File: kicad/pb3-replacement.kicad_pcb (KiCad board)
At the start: 2 copper layers, 0 parts

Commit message: Create PB-3 PCB layout and KiBot outputs
Co-authored-by: donnels <14863623+donnels@users.noreply.github.com>
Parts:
- added BT1: LiPo_3.7V_500-1500mAh, Battery:LiPo_68x17.8mm, B.Cu at (151.0, 108.9)
- added J1: USB_C_5V_IN, Connector_USB:USB_C_Receptacle_USB2.0, F.Cu at (104.0, 108.9)
- added J2: AIWA_DECK_2.4V, Connector:Conn_01x02_Pin, F.Cu at (163.0, 108.9)
- added Q1: FS8205A, Package_TO_SOT_SMD:SOT-23-6, F.Cu at (131.0, 108.9)
- added U1: TP4056, Package_SO:SOIC-8_3.9x4.9mm_P1.27mm, F.Cu at (115.0, 108.9)
- added U2: DW01A, Package_TO_SOT_SMD:SOT-23-6, F.Cu at (124.0, 108.9)
- added U3: TPS61023_2.4V, Regulator_Switching:SOT-23-5, F.Cu at (141.0, 108.9)
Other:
- board outline added: 68 x 17.8 mm
- board text added: "68 x 17.8 mm"
- board text added: "AIWA PB-3 1S LiPo / 2.4 V"
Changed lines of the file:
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@@
-(kicad_pcb (version 20240108) (generator "GitHub Copilot")
-  (general (thickness 1.6))
+(kicad_pcb (version 20240108) (generator pcbnew)
+  (general (thickness 0.8))
   (paper "A4")
   (title_block
-    (title "PB-3 Replacement Gauge")
+    (title "AIWA PB-3 LiPo Replacement")
     (company "AIWA HS-PC202MII")
-    (rev "V0.1")
-    (comment 1 "Outline only. Populate once donor measurements confirmed."))
+    (rev "0.1")
+    (comment 1 "68 x 17.8 mm prototype board; verify connector pinout before fabrication"))
   (layers
     (0 "F.Cu" signal)
     (31 "B.Cu" signal)
-    (34 "Edge.Cuts" user))
+    (36 "B.SilkS" user "b.silkscreen")
+    (37 "F.SilkS" user "f.silkscreen")
+    (44 "Edge.Cuts" user))
   (setup
-    (stackup
-      (layer "F.Cu" (type "signal"))
-      (layer "dielectric 1" (type "dielectric") (thickness 1.5))
-      (layer "B.Cu" (type "signal")))
-    (grid_origin 0 0)
-  )
+    (pad_to_mask_clearance 0)
+    (allow_soldermask_bridges_in_footprints no)
+    (pcbplotparams
+      (layerselection 0x00010fc_ffffffff)
+      (plot_on_all_layers_selection 0x0000000_00000000)
+      (disableapertmacros no)
+      (usegerberextensions yes)
+      (usegerberattributes yes)
+      (usegerberadvancedattributes yes)
+      (creategerberjobfile yes)
+      (dashed_line_dash_ratio 12)
+      (dashed_line_gap_ratio 3)
+      (svgprecision 4)
+      (plotframeref no)
+      (viasonmask no)
+      (mode 1)
+      (useauxorigin no)
+      (hpglpennumber 1)
+      (hpglpenspeed 20)
+      (hpglpendiameter 15)
+      (psnegative no)
+      (psa4output no)
+      (plotreference yes)
+      (plotvalue yes)
+      (plotfptext yes)
+      (plotinvisibletext no)
+      (sketchpadsonfab no)
+      (subtractmaskfromsilk no)
+      (outputformat 1)
+      (mirror no)
+      (drillshape 0)
+      (scaleselection 1)
+      (outputdirectory "fabrication/")))
+  (gr_rect (start 100 100) (end 168 117.8) (stroke (width 0.15) (type default)) (fill none) (layer "Edge.Cuts"))
+  (gr_text "AIWA PB-3  1S LiPo / 2.4 V" (at 134 102.2) (layer "F.SilkS")
+    (effects (font (size 1 1) (thickness 0.15))))
+  (gr_text "68 x 17.8 mm" (at 134 115.8) (layer "B.SilkS")
+    (effects (font (size 0.8 0.8) (thickness 0.12)) (justify mirror)))
+  (footprint "Connector_USB:USB_C_Receptacle_USB2.0" (layer "F.Cu") (at 104 108.9)
+    (property "Reference" "J1" (at 0 -4 0) (layer "F.SilkS") (effects (font (size 1 1) (thickness 0.15))))
+    (property "Value" "USB_C_5V_IN" (at 0 4 0) (layer "F.Fab") hide (effects (font (size 1 1) (thickness 0.15))))
+    (fp_rect (start -3 -2.5) (end 3 2.5) (stroke (width 0.15) (type default)) (fill none) (layer "F.SilkS"))
+    (pad "1" thru_hole rect (at -1.5 0) (size 1.8 1.8) (drill 1) (layers "*.Cu" "*.Mask"))
+    (pad "2" thru_hole circle (at 1.5 0) (size 1.8 1.8) (drill 1) (layers "*.Cu" "*.Mask")))
+  (footprint "Package_SO:SOIC-8_3.9x4.9mm_P1.27mm" (layer "F.Cu") (at 115 108.9)
+    (property "Reference" "U1" (at 0 -3.2 0) (layer "F.SilkS") (effects (font (size 1 1) (thickness 0.15))))
+    (property "Value" "TP4056" (at 0 3.2 0) (layer "F.Fab") hide (effects (font (size 1 1) (thickness 0.15))))
+    (fp_rect (start -2.4 -2.1) (end 2.4 2.1) (stroke (width 0.15) (type default)) (fill none) (layer "F.SilkS"))
+    (pad "1" smd roundrect (at -2.4 -1.905) (size 1.5 0.6) (layers "F.Cu" "F.Paste" "F.Mask") (roundrect_rratio 0.2))
+    (pad "2" smd roundrect (at -2.4 -0.635) (size 1.5 0.6) (layers "F.Cu" "F.Paste" "F.Mask") (roundrect_rratio 0.2))
+    (pad "3" smd roundrect (at -2.4 0.635) (size 1.5 0.6) (layers "F.Cu" "F.Paste" "F.Mask") (roundrect_rratio 0.2))
+    (pad "4" smd roundrect (at -2.4 1.905) (size 1.5 0.6) (layers "F.Cu" "F.Paste" "F.Mask") (roundrect_rratio 0.2))
+    (pad "5" smd roundrect (at 2.4 1.905) (size 1.5 0.6) (layers "F.Cu" "F.Paste" "F.Mask") (roundrect_rratio 0.2))
+    (pad "6" smd roundrect (at 2.4 0.635) (size 1.5 0.6) (layers "F.Cu" "F.Paste" "F.Mask") (roundrect_rratio 0.2))
+    (pad "7" smd roundrect (at 2.4 -0.635) (size 1.5 0.6) (layers "F.Cu" "F.Paste" "F.Mask") (roundrect_rratio 0.2))
+    (pad "8" smd roundrect (at 2.4 -1.905) (size 1.5 0.6) (layers "F.Cu" "F.Paste" "F.Mask") (roundrect_rratio 0.2)))
+  (footprint "Package_TO_SOT_SMD:SOT-23-6" (layer "F.Cu") (at 124 108.9)
+    (property "Reference" "U2" (at 0 -2.5 0) (layer "F.SilkS") (effects (font (size 1 1) (thickness 0.15))))
+    (property "Value" "DW01A" (at 0 2.5 0) (layer "F.Fab") hide (effects (font (size 1 1) (thickness 0.15))))
+    (fp_rect (start -1.6 -1.3) (end 1.6 1.3) (stroke (width 0.15) (type default)) (fill none) (layer "F.SilkS"))
+    (pad "1" smd roundrect (at -1.1 -1.1) (size 1.2 0.6) (layers "F.Cu" "F.Paste" "F.Mask") (roundrect_rratio 0.2))
+    (pad "2" smd roundrect (at -1.1 0) (size 1.2 0.6) (layers "F.Cu" "F.Paste" "F.Mask") (roundrect_rratio 0.2))
+    (pad "3" smd roundrect (at -1.1 1.1) (size 1.2 0.6) (layers "F.Cu" "F.Paste" "F.Mask") (roundrect_rratio 0.2))
+    (pad "4" smd roundrect (at 1.1 1.1) (size 1.2 0.6) (layers "F.Cu" "F.Paste" "F.Mask") (roundrect_rratio 0.2))
+    (pad "5" smd roundrect (at 1.1 0) (size 1.2 0.6) (layers "F.Cu" "F.Paste" "F.Mask") (roundrect_rratio 0.2))
+    (pad "6" smd roundrect (at 1.1 -1.1) (size 1.2 0.6) (layers "F.Cu" "F.Paste" "F.Mask") (roundrect_rratio 0.2)))
+  (footprint "Package_TO_SOT_SMD:SOT-23-6" (layer "F.Cu") (at 131 108.9)
+    (property "Reference" "Q1" (at 0 -2.5 0) (layer "F.SilkS") (effects (font (size 1 1) (thickness 0.15))))
+    (property "Value" "FS8205A" (at 0 2.5 0) (layer "F.Fab") hide (effects (font (size 1 1) (thickness 0.15))))
+    (fp_rect (start -1.6 -1.3) (end 1.6 1.3) (stroke (width 0.15) (type default)) (fill none) (layer "F.SilkS"))
+    (pad "1" smd roundrect (at -1.1 -1.1) (size 1.2 0.6) (layers "F.Cu" "F.Paste" "F.Mask") (roundrect_rratio 0.2))
+    (pad "2" smd roundrect (at -1.1 0) (size 1.2 0.6) (layers "F.Cu" "F.Paste" "F.Mask") (roundrect_rratio 0.2))
+    (pad "3" smd roundrect (at -1.1 1.1) (size 1.2 0.6) (layers "F.Cu" "F.Paste" "F.Mask") (roundrect_rratio 0.2))
+    (pad "4" smd roundrect (at 1.1 1.1) (size 1.2 0.6) (layers "F.Cu" "F.Paste" "F.Mask") (roundrect_rratio 0.2))
+    (pad "5" smd roundrect (at 1.1 0) (size 1.2 0.6) (layers "F.Cu" "F.Paste" "F.Mask") (roundrect_rratio 0.2))
+    (pad "6" smd roundrect (at 1.1 -1.1) (size 1.2 0.6) (layers "F.Cu" "F.Paste" "F.Mask") (roundrect_rratio 0.2)))
+  (footprint "Regulator_Switching:SOT-23-5" (layer "F.Cu") (at 141 108.9)
+    (property "Reference" "U3" (at 0 -2.5 0) (layer "F.SilkS") (effects (font (size 1 1) (thickness 0.15))))
+    (property "Value" "TPS61023_2.4V" (at 0 2.5 0) (layer "F.Fab") hide (effects (font (size 1 1) (thickness 0.15))))
+    (fp_rect (start -1.6 -1.3) (end 1.6 1.3) (stroke (width 0.15) (type default)) (fill none) (layer "F.SilkS"))
+    (pad "1" smd roundrect (at -1.1 -1.1) (size 1.2 0.6) (layers "F.Cu" "F.Paste" "F.Mask") (roundrect_rratio 0.2))
+    (pad "2" smd roundrect (at -1.1 0) (size 1.2 0.6) (layers "F.Cu" "F.Paste" "F.Mask") (roundrect_rratio 0.2))
+    (pad "3" smd roundrect (at -1.1 1.1) (size 1.2 0.6) (layers "F.Cu" "F.Paste" "F.Mask") (roundrect_rratio 0.2))
+    (pad "4" smd roundrect (at 1.1 1.1) (size 1.2 0.6) (layers "F.Cu" "F.Paste" "F.Mask") (roundrect_rratio 0.2))
+    (pad "5" smd roundrect (at 1.1 0) (size 1.2 0.6) (layers "F.Cu" "F.Paste" "F.Mask") (roundrect_rratio 0.2)))
+  (footprint "Connector:Conn_01x02_Pin" (layer "F.Cu") (at 163 108.9)
+    (property "Reference" "J2" (at 0 -3 0) (layer "F.SilkS") (effects (font (size 1 1) (thickness 0.15))))
+    (property "Value" "AIWA_DECK_2.4V" (at 0 3 0) (layer "F.Fab") hide (effects (font (size 1 1) (thickness 0.15))))
+    (fp_rect (start -2 -2) (end 2 2) (stroke (width 0.15) (type default)) (fill none) (layer "F.SilkS"))
+    (pad "1" thru_hole rect (at 0 -1.27) (size 2 2) (drill 1) (layers "*.Cu" "*.Mask"))
+    (pad "2" thru_hole circle (at 0 1.27) (size 2 2) (drill 1) (layers "*.Cu" "*.Mask")))
+  (footprint "Battery:LiPo_68x17.8mm" (layer "B.Cu") (at 151 108.9)
+    (property "Reference" "BT1" (at 0 -5.5 0) (layer "B.SilkS") (effects (font (size 1 1) (thickness 0.15)) (justify mirror)))
+    (property "Value" "LiPo_3.7V_500-1500mAh" (at 0 5.5 0) (layer "B.Fab") hide (effects (font (size 1 1) (thickness 0.15)) (justify mirror)))
+    (fp_rect (start -8 -3.5) (end 8 3.5) (stroke (width 0.15) (type default)) (fill none) (layer "B.SilkS"))
+    (pad "1" thru_hole rect (at -6 0) (size 2 2) (drill 1) (layers "*.Cu" "*.Mask"))
+    (pad "2" thru_hole circle (at 6 0) (size 2 2) (drill 1) (layers "*.Cu" "*.Mask")))
 )

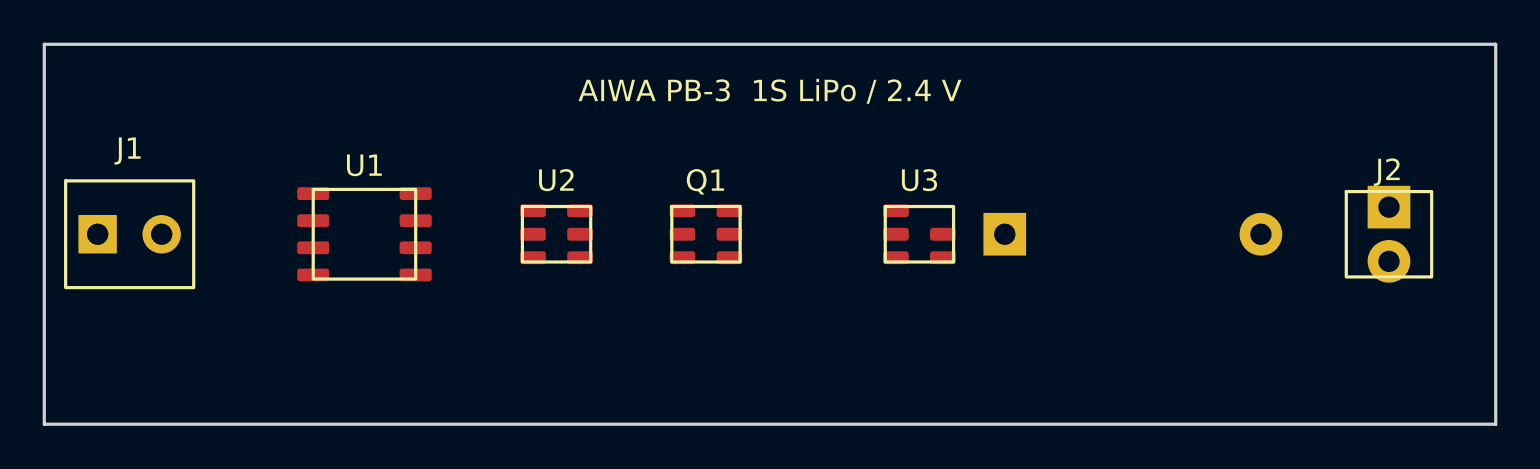
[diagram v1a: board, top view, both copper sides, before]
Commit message: Finalize DRC-clean PB-3 board layout
Co-authored-by: donnels <14863623+donnels@users.noreply.github.com>
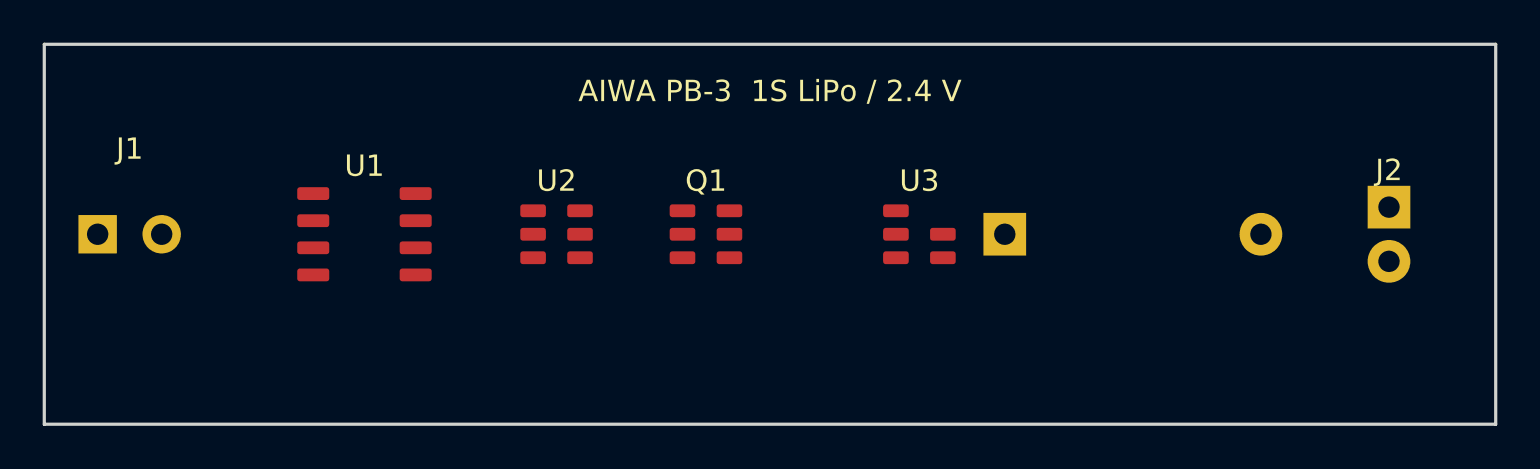
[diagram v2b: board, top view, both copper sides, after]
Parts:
- BT1: footprint Battery:LiPo_68x17.8mm -> PB3_LIPO_68x17.8mm
- J1: footprint Connector_USB:USB_C_Receptacle_USB2.0 -> PB3_USB_C
- J2: footprint Connector:Conn_01x02_Pin -> PB3_DECK_CONNECTOR
- Q1: footprint Package_TO_SOT_SMD:SOT-23-6 -> PB3_FS8205A_SOT23-6
- U1: footprint Package_SO:SOIC-8_3.9x4.9mm_P1.27mm -> PB3_TP4056_SOIC8
- U2: footprint Package_TO_SOT_SMD:SOT-23-6 -> PB3_DW01A_SOT23-6
- U3: footprint Regulator_Switching:SOT-23-5 -> PB3_TPS61023_SOT23-5
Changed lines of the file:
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@@
     (36 "B.SilkS" user "b.silkscreen")
     (37 "F.SilkS" user "f.silkscreen")
+    (49 "F.Fab" user)
     (44 "Edge.Cuts" user))
   (setup
@@
   (gr_text "68 x 17.8 mm" (at 134 115.8) (layer "B.SilkS")
     (effects (font (size 0.8 0.8) (thickness 0.12)) (justify mirror)))
-  (footprint "Connector_USB:USB_C_Receptacle_USB2.0" (layer "F.Cu") (at 104 108.9)
+  (footprint "PB3_USB_C" (layer "F.Cu") (at 104 108.9)
     (property "Reference" "J1" (at 0 -4 0) (layer "F.SilkS") (effects (font (size 1 1) (thickness 0.15))))
     (property "Value" "USB_C_5V_IN" (at 0 4 0) (layer "F.Fab") hide (effects (font (size 1 1) (thickness 0.15))))
-    (fp_rect (start -3 -2.5) (end 3 2.5) (stroke (width 0.15) (type default)) (fill none) (layer "F.SilkS"))
+    (fp_rect (start -3 -2.5) (end 3 2.5) (stroke (width 0.15) (type default)) (fill none) (layer "F.Fab"))
     (pad "1" thru_hole rect (at -1.5 0) (size 1.8 1.8) (drill 1) (layers "*.Cu" "*.Mask"))
     (pad "2" thru_hole circle (at 1.5 0) (size 1.8 1.8) (drill 1) (layers "*.Cu" "*.Mask")))
-  (footprint "Package_SO:SOIC-8_3.9x4.9mm_P1.27mm" (layer "F.Cu") (at 115 108.9)
+  (footprint "PB3_TP4056_SOIC8" (layer "F.Cu") (at 115 108.9)
     (property "Reference" "U1" (at 0 -3.2 0) (layer "F.SilkS") (effects (font (size 1 1) (thickness 0.15))))
     (property "Value" "TP4056" (at 0 3.2 0) (layer "F.Fab") hide (effects (font (size 1 1) (thickness 0.15))))
-    (fp_rect (start -2.4 -2.1) (end 2.4 2.1) (stroke (width 0.15) (type default)) (fill none) (layer "F.SilkS"))
+    (fp_rect (start -2.4 -2.1) (end 2.4 2.1) (stroke (width 0.15) (type default)) (fill none) (layer "F.Fab"))
     (pad "1" smd roundrect (at -2.4 -1.905) (size 1.5 0.6) (layers "F.Cu" "F.Paste" "F.Mask") (roundrect_rratio 0.2))
     (pad "2" smd roundrect (at -2.4 -0.635) (size 1.5 0.6) (layers "F.Cu" "F.Paste" "F.Mask") (roundrect_rratio 0.2))
@@
     (pad "7" smd roundrect (at 2.4 -0.635) (size 1.5 0.6) (layers "F.Cu" "F.Paste" "F.Mask") (roundrect_rratio 0.2))
     (pad "8" smd roundrect (at 2.4 -1.905) (size 1.5 0.6) (layers "F.Cu" "F.Paste" "F.Mask") (roundrect_rratio 0.2)))
-  (footprint "Package_TO_SOT_SMD:SOT-23-6" (layer "F.Cu") (at 124 108.9)
+  (footprint "PB3_DW01A_SOT23-6" (layer "F.Cu") (at 124 108.9)
     (property "Reference" "U2" (at 0 -2.5 0) (layer "F.SilkS") (effects (font (size 1 1) (thickness 0.15))))
     (property "Value" "DW01A" (at 0 2.5 0) (layer "F.Fab") hide (effects (font (size 1 1) (thickness 0.15))))
-    (fp_rect (start -1.6 -1.3) (end 1.6 1.3) (stroke (width 0.15) (type default)) (fill none) (layer "F.SilkS"))
+    (fp_rect (start -1.6 -1.3) (end 1.6 1.3) (stroke (width 0.15) (type default)) (fill none) (layer "F.Fab"))
     (pad "1" smd roundrect (at -1.1 -1.1) (size 1.2 0.6) (layers "F.Cu" "F.Paste" "F.Mask") (roundrect_rratio 0.2))
     (pad "2" smd roundrect (at -1.1 0) (size 1.2 0.6) (layers "F.Cu" "F.Paste" "F.Mask") (roundrect_rratio 0.2))
@@
     (pad "5" smd roundrect (at 1.1 0) (size 1.2 0.6) (layers "F.Cu" "F.Paste" "F.Mask") (roundrect_rratio 0.2))
     (pad "6" smd roundrect (at 1.1 -1.1) (size 1.2 0.6) (layers "F.Cu" "F.Paste" "F.Mask") (roundrect_rratio 0.2)))
-  (footprint "Package_TO_SOT_SMD:SOT-23-6" (layer "F.Cu") (at 131 108.9)
+  (footprint "PB3_FS8205A_SOT23-6" (layer "F.Cu") (at 131 108.9)
     (property "Reference" "Q1" (at 0 -2.5 0) (layer "F.SilkS") (effects (font (size 1 1) (thickness 0.15))))
     (property "Value" "FS8205A" (at 0 2.5 0) (layer "F.Fab") hide (effects (font (size 1 1) (thickness 0.15))))
-    (fp_rect (start -1.6 -1.3) (end 1.6 1.3) (stroke (width 0.15) (type default)) (fill none) (layer "F.SilkS"))
+    (fp_rect (start -1.6 -1.3) (end 1.6 1.3) (stroke (width 0.15) (type default)) (fill none) (layer "F.Fab"))
     (pad "1" smd roundrect (at -1.1 -1.1) (size 1.2 0.6) (layers "F.Cu" "F.Paste" "F.Mask") (roundrect_rratio 0.2))
     (pad "2" smd roundrect (at -1.1 0) (size 1.2 0.6) (layers "F.Cu" "F.Paste" "F.Mask") (roundrect_rratio 0.2))
@@
     (pad "5" smd roundrect (at 1.1 0) (size 1.2 0.6) (layers "F.Cu" "F.Paste" "F.Mask") (roundrect_rratio 0.2))
     (pad "6" smd roundrect (at 1.1 -1.1) (size 1.2 0.6) (layers "F.Cu" "F.Paste" "F.Mask") (roundrect_rratio 0.2)))
-  (footprint "Regulator_Switching:SOT-23-5" (layer "F.Cu") (at 141 108.9)
+  (footprint "PB3_TPS61023_SOT23-5" (layer "F.Cu") (at 141 108.9)
     (property "Reference" "U3" (at 0 -2.5 0) (layer "F.SilkS") (effects (font (size 1 1) (thickness 0.15))))
     (property "Value" "TPS61023_2.4V" (at 0 2.5 0) (layer "F.Fab") hide (effects (font (size 1 1) (thickness 0.15))))
-    (fp_rect (start -1.6 -1.3) (end 1.6 1.3) (stroke (width 0.15) (type default)) (fill none) (layer "F.SilkS"))
+    (fp_rect (start -1.6 -1.3) (end 1.6 1.3) (stroke (width 0.15) (type default)) (fill none) (layer "F.Fab"))
     (pad "1" smd roundrect (at -1.1 -1.1) (size 1.2 0.6) (layers "F.Cu" "F.Paste" "F.Mask") (roundrect_rratio 0.2))
     (pad "2" smd roundrect (at -1.1 0) (size 1.2 0.6) (layers "F.Cu" "F.Paste" "F.Mask") (roundrect_rratio 0.2))
@@
     (pad "4" smd roundrect (at 1.1 1.1) (size 1.2 0.6) (layers "F.Cu" "F.Paste" "F.Mask") (roundrect_rratio 0.2))
     (pad "5" smd roundrect (at 1.1 0) (size 1.2 0.6) (layers "F.Cu" "F.Paste" "F.Mask") (roundrect_rratio 0.2)))
-  (footprint "Connector:Conn_01x02_Pin" (layer "F.Cu") (at 163 108.9)
+  (footprint "PB3_DECK_CONNECTOR" (layer "F.Cu") (at 163 108.9)
     (property "Reference" "J2" (at 0 -3 0) (layer "F.SilkS") (effects (font (size 1 1) (thickness 0.15))))
     (property "Value" "AIWA_DECK_2.4V" (at 0 3 0) (layer "F.Fab") hide (effects (font (size 1 1) (thickness 0.15))))
-    (fp_rect (start -2 -2) (end 2 2) (stroke (width 0.15) (type default)) (fill none) (layer "F.SilkS"))
+    (fp_rect (start -2 -2) (end 2 2) (stroke (width 0.15) (type default)) (fill none) (layer "F.Fab"))
     (pad "1" thru_hole rect (at 0 -1.27) (size 2 2) (drill 1) (layers "*.Cu" "*.Mask"))
     (pad "2" thru_hole circle (at 0 1.27) (size 2 2) (drill 1) (layers "*.Cu" "*.Mask")))
-  (footprint "Battery:LiPo_68x17.8mm" (layer "B.Cu") (at 151 108.9)
+  (footprint "PB3_LIPO_68x17.8mm" (layer "B.Cu") (at 151 108.9)
     (property "Reference" "BT1" (at 0 -5.5 0) (layer "B.SilkS") (effects (font (size 1 1) (thickness 0.15)) (justify mirror)))
     (property "Value" "LiPo_3.7V_500-1500mAh" (at 0 5.5 0) (layer "B.Fab") hide (effects (font (size 1 1) (thickness 0.15)) (justify mirror)))

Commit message: Route PB-3 PCB nets/traces; add copper for power path
Co-authored-by: donnels <14863623+donnels@users.noreply.github.com>
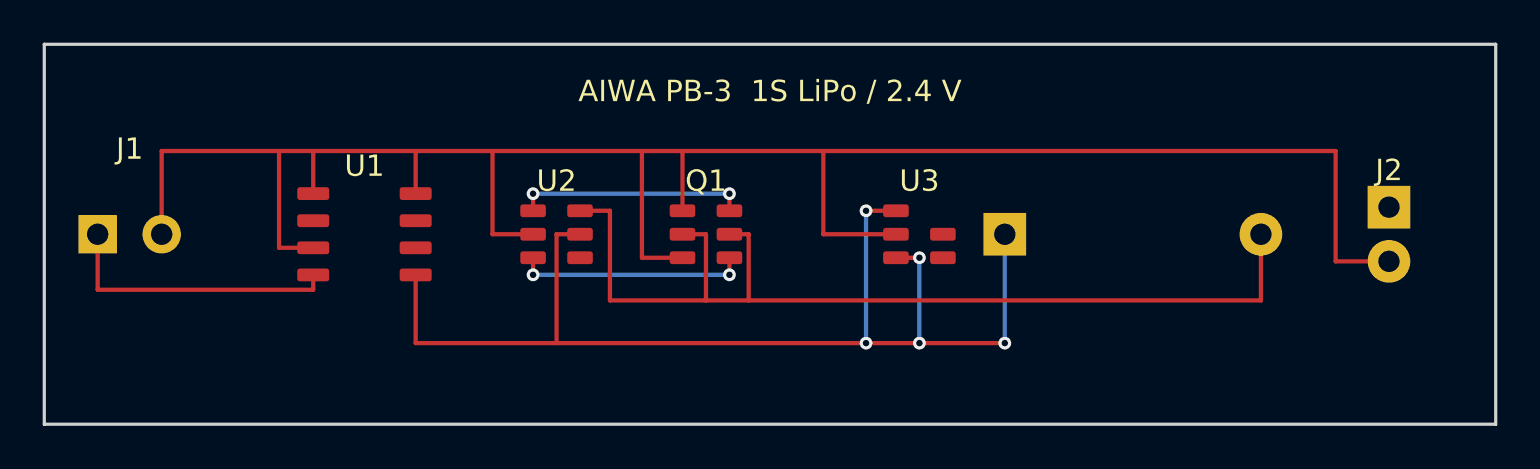
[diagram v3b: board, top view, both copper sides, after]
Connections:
- BT1 pad 1: (no net) -> VBAT
- BT1 pad 2: (no net) -> VBAT_RAW_NEG
- J1 pad 1: (no net) -> VBUS
- J1 pad 2: (no net) -> GND
- J2 pad 1: (no net) -> NC_VOUT
- J2 pad 2: (no net) -> GND
- Q1 pad 1: (no net) -> GND
- Q1 pad 2: (no net) -> VBAT_RAW_NEG
- Q1 pad 3: (no net) -> GND
- Q1 pad 4: (no net) -> OC
- Q1 pad 5: (no net) -> VBAT_RAW_NEG
- Q1 pad 6: (no net) -> OD
- U1 pad 1: (no net) -> GND
- U1 pad 2: (no net) -> NC_PROG
- U1 pad 3: (no net) -> GND
- U1 pad 4: (no net) -> VBUS
- U1 pad 5: (no net) -> VBAT
- U1 pad 6: (no net) -> NC_STDBY
- U1 pad 7: (no net) -> NC_CHRG
- U1 pad 8: (no net) -> GND
- U2 pad 1: (no net) -> OD
- U2 pad 2: (no net) -> GND
- U2 pad 3: (no net) -> OC
- U2 pad 4: (no net) -> NC_TD
- U2 pad 5: (no net) -> VBAT
- U2 pad 6: (no net) -> VBAT_RAW_NEG
- U3 pad 1: (no net) -> VBAT
- U3 pad 2: (no net) -> GND
- U3 pad 3: (no net) -> VBAT
- U3 pad 4: (no net) -> NC_FB
- U3 pad 5: (no net) -> NC_SW
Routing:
- net GND: track 0.00 -> 99.5 mm
- net VBAT: track 0.00 -> 54.8 mm, vias 0 -> 5
- net VBAT_RAW_NEG: track 0.00 -> 47.4 mm
- net VBUS: track 0.00 -> 13.4 mm
- net OD: track 0.00 -> 10.8 mm, vias 0 -> 2
- net OC: track 0.00 -> 10.8 mm, vias 0 -> 2
